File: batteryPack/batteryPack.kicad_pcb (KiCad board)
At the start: 2 copper layers, 210.8 x 83 mm, 38 parts, among them J1 Mirco USB, J10 B1+, J11 B1-, J12 B2-, J13 B1+, J14 B1-, J15 B2+, J16 B2-, J2 B1+, J3 B1-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

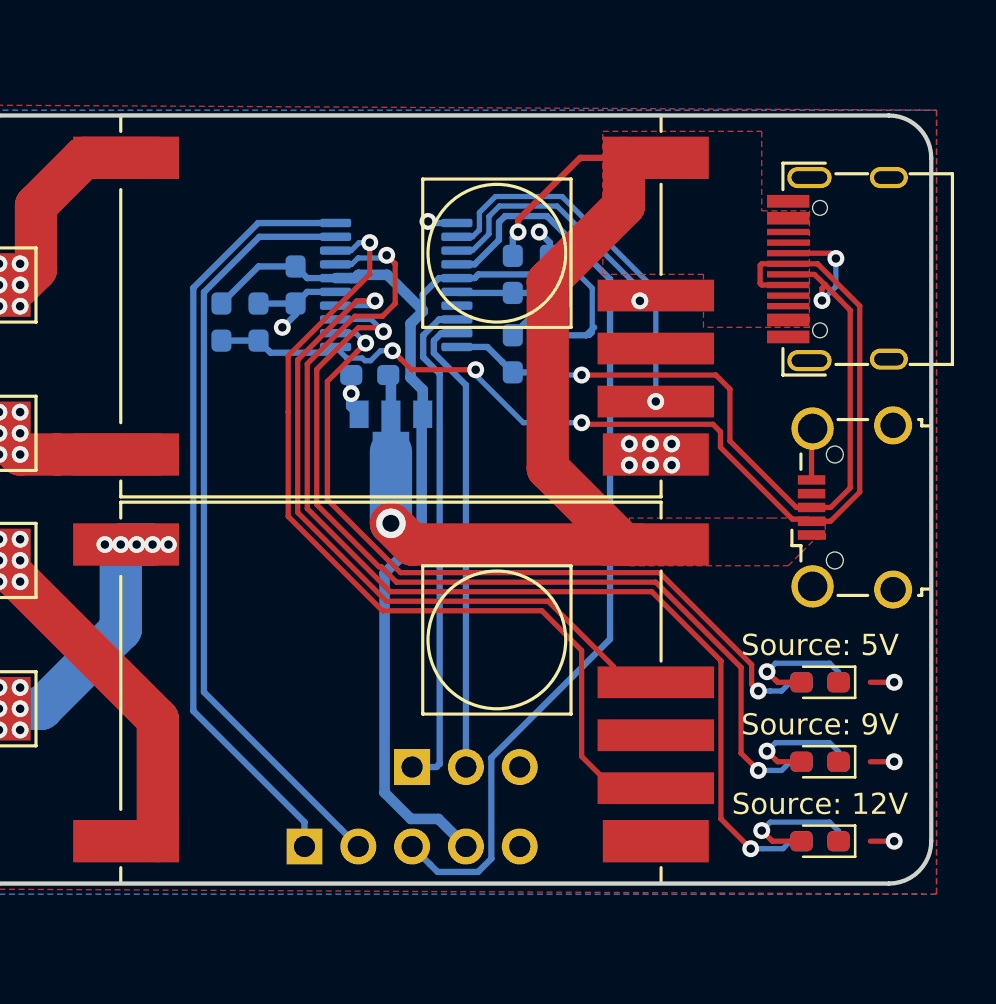
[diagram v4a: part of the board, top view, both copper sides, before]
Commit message: Add battery voltage signalization
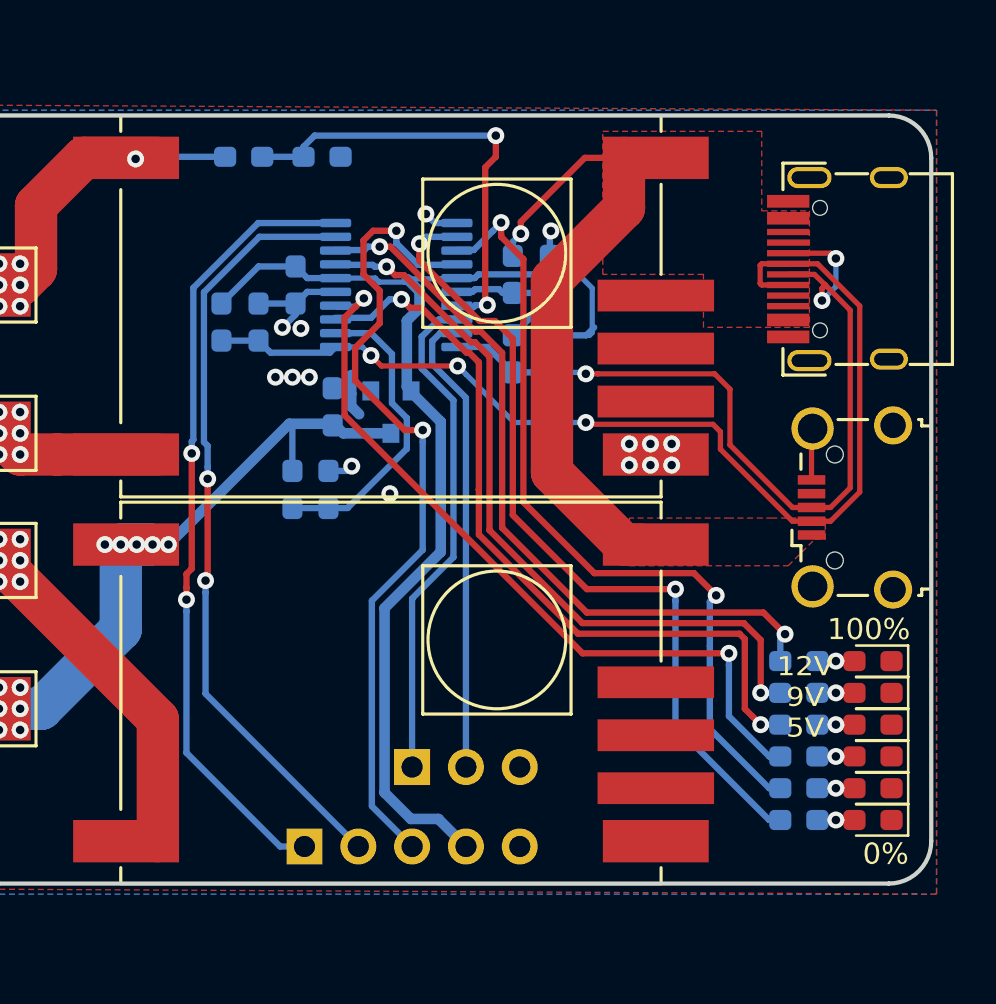
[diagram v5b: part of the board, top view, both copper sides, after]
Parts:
- added D4: LED_40%, LED_SMD:LED_0603_1608Metric_Pad1.05x0.95mm_HandSolder, F.Cu at (231.2, 82.2)
- added D5: LED_20%, LED_SMD:LED_0603_1608Metric_Pad1.05x0.95mm_HandSolder, F.Cu at (231.2, 83.8)
- added D6: LED_0%, LED_SMD:LED_0603_1608Metric_Pad1.05x0.95mm_HandSolder, F.Cu at (231.2, 85.2)
- added R10: 10k, Resistor_SMD:R_0603_1608Metric_Pad1.05x0.95mm_HandSolder, B.Cu at (203.8, 69.7)
- added R11: 20k, Resistor_SMD:R_0603_1608Metric_Pad1.05x0.95mm_HandSolder, B.Cu at (205.6, 69.7)
- added R12: 10k, Resistor_SMD:R_0603_1608Metric_Pad1.05x0.95mm_HandSolder, B.Cu at (201.6, 54.0)
- added R13: 20k, Resistor_SMD:R_0603_1608Metric_Pad1.05x0.95mm_HandSolder, B.Cu at (205.2, 54.0)
- added R14: 1k, Resistor_SMD:R_0603_1608Metric_Pad1.05x0.95mm_HandSolder, B.Cu at (227.8, 82.2)
- added R15: 1k, Resistor_SMD:R_0603_1608Metric_Pad1.05x0.95mm_HandSolder, B.Cu at (227.8, 83.8)
- added R16: 1k, Resistor_SMD:R_0603_1608Metric_Pad1.05x0.95mm_HandSolder, B.Cu at (227.8, 85.2)
- U3: value HT7533-1 -> XC6206P332MR; footprint Package_TO_SOT_SMD:SOT-89-3 -> Package_TO_SOT_SMD:SOT-23
- moved D3 8.86 mm to (231.2, 77.8)
- moved R7 8.56 mm to (227.8, 77.8)
- moved D2 4.10 mm to (231.2, 79.2)
- moved R6 3.40 mm to (227.8, 79.2)
- moved D1 3.20 mm to (231.2, 80.8)
- moved C2 2.30 mm to (205.8, 65.8), turned to 270 degrees
- moved R5 2.24 mm to (227.8, 80.8)
- moved U3 1.75 mm to (208.5, 66.0)
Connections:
- net Net-(J13-Pad1) renamed BAT1+
- C2 pad 2: VBUS -> BAT2+
- J15 pad 1: Net-(J15-Pad1) -> BAT2+
- U1 pad 6: B1_CH -> (no net)
- U1 pad 7: B1_F -> (no net)
- U2 pad 12: Net-(R5-Pad1) -> BAT2_V
- U2 pad 13: Net-(R6-Pad1) -> Net-(R5-Pad1)
- U2 pad 14: B2_F -> Net-(R14-Pad1)
- U2 pad 17: Net-(R7-Pad1) -> Net-(R6-Pad1)
- U2 pad 18: B2_CH -> Net-(R7-Pad1)
- U2 pad 2: B1_CH -> Net-(R16-Pad1)
- U2 pad 3: B1_F -> Net-(R15-Pad1)
- U2 pad 7: (no net) -> BAT1_V
- U3 pad 2: VBUS -> +3V3
- U3 pad 3: +3V3 -> BAT2+
- U4 pad 3: Net-(J15-Pad1) -> BAT2+
- U4 pad 6: B2_CH -> (no net)
- U4 pad 7: B2_F -> (no net)
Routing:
- net B2_CH: track 39.9 -> 0.00 mm, vias 1 -> 0
- net Net-(R16-Pad1): track 0.00 -> 39.3 mm, vias 0 -> 2
- net Net-(R15-Pad1): track 0.00 -> 38.0 mm, vias 0 -> 2
- net Net-(R14-Pad1): track 0.00 -> 36.3 mm, vias 0 -> 2
- net B2_F: track 32.6 -> 0.00 mm, vias 1 -> 0
- net BAT2+: track 0.00 -> 28.2 mm, vias 0 -> 14
- net BAT1_V: track 0.00 -> 21.5 mm, vias 0 -> 2
- net B1_CH: track 19.7 -> 0.00 mm, vias 1 -> 0
- net VBUS: track 46.9 -> 29.8 mm, vias 2 -> 1
- net Net-(R7-Pad1): track 51.7 -> 35.1 mm
- net BAT2_V: track 0.00 -> 14.4 mm
- net B1_F: track 13.5 -> 0.00 mm, vias 1 -> 0
- net Net-(J15-Pad1): track 12.8 -> 0.00 mm, vias 14 -> 0
- net Net-(R6-Pad1): track 43.5 -> 35.7 mm
- net RST: track 44.1 -> 38.7 mm, vias 0 -> 2
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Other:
- board text added: "0%"
- board text added: "100%"
- board text added: "12V 9V 5V"
- board text removed: "Source: 12V"
- board text removed: "Source: 5V"
- board text removed: "Source: 9V"

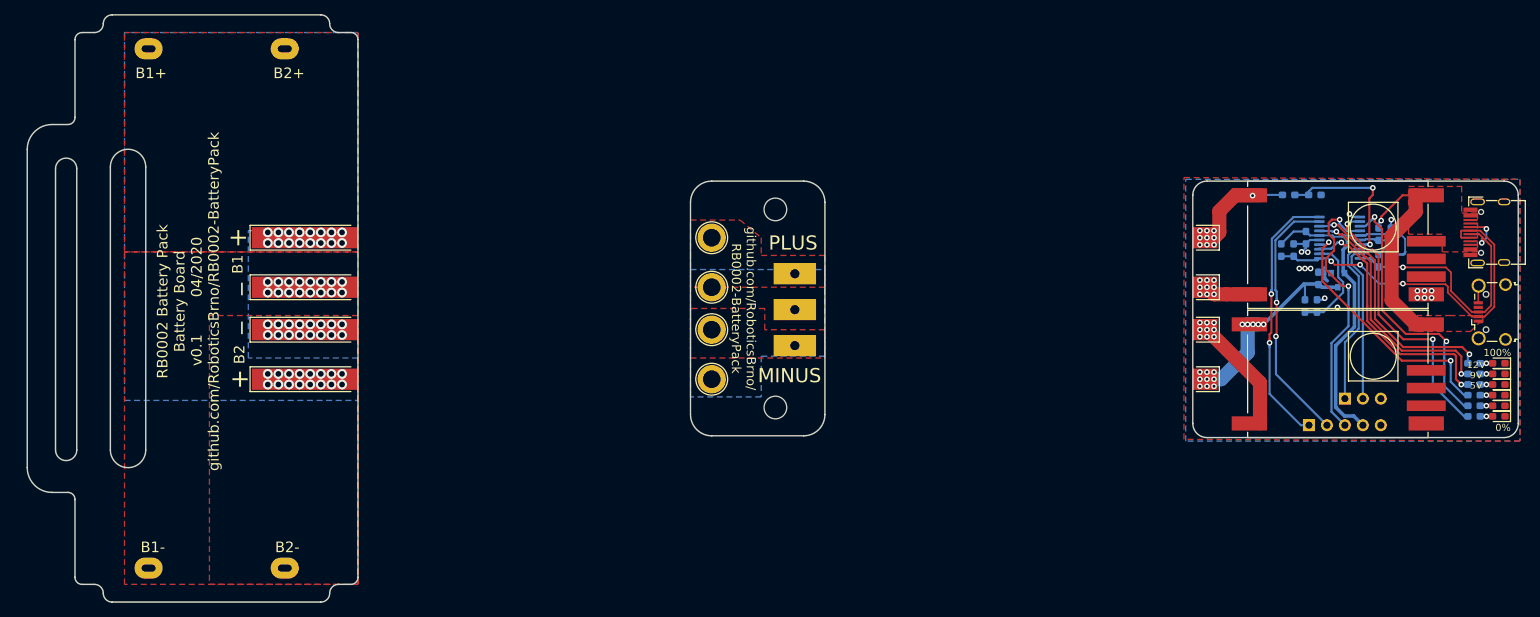
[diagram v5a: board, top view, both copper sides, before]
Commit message: Add silkscreen text + LICENSE
- add version info text to Charger board
- add +/- text for Charger and Connector board
- add license Creative Commons BY-SA 4.0
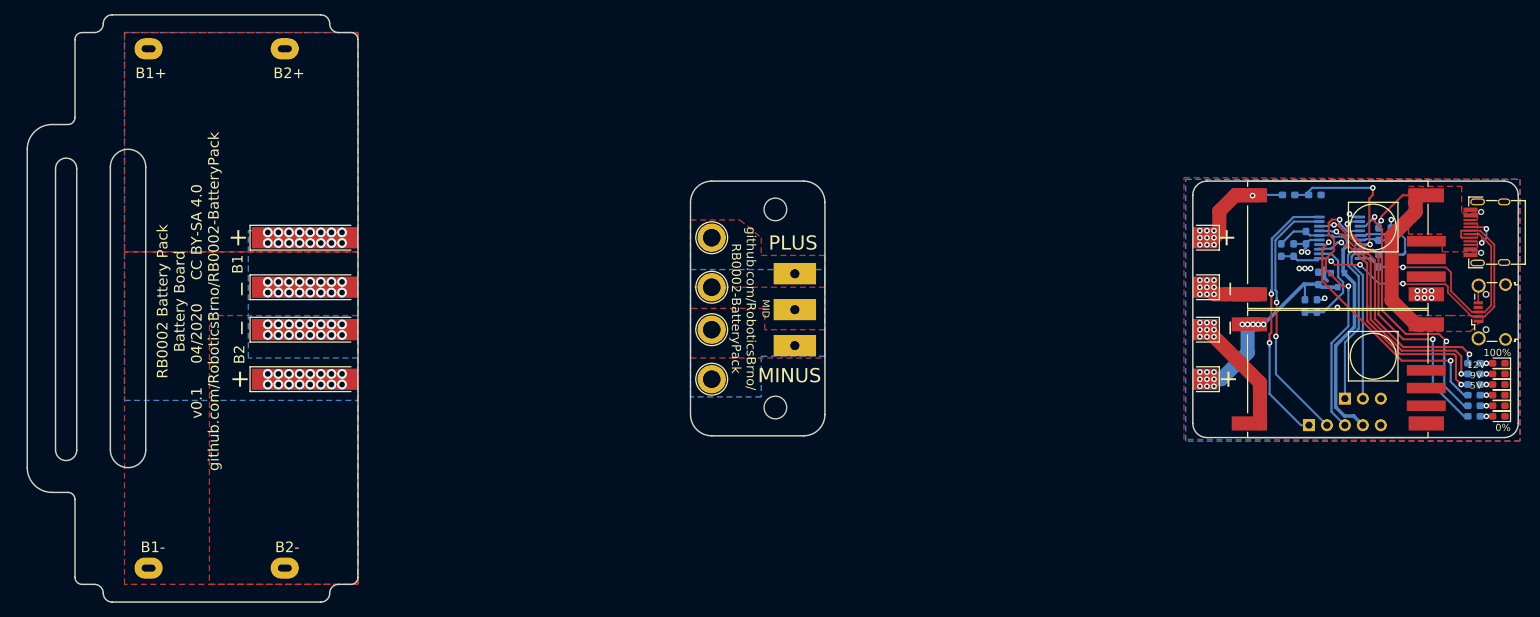
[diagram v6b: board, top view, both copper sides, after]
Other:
- rule trace_min: 0.2 -> 0.1
- rule via_min_size: 0.4 -> 0.35
- board text added: "-"
- board text added: "MID"
- board text added: "RB0002 Battery Pack Battery Board v0.1 04/2020 CC BY-SA 4.0 github.com/RoboticsBrno/RB0002-BatteryPack"
- board text added: "RB0002 Battery Pack Charger v0.1 04/2020"
- board text added: "github.com/RoboticsBrno/ RB0002-BatteryPack CC BY-SA 4.0"
- board text removed: "RB0002 Battery Pack Battery Board v0.1 04/2020 github.com/RoboticsBrno/RB0002-BatteryPack"
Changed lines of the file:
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@@
-(kicad_pcb (version 20171130) (host pcbnew 5.1.5+dfsg1-2build2)
+(kicad_pcb (version 20171130) (host pcbnew "(5.1.5)-3")
   (general
     (thickness 1.6)
-    (drawings 138)
+    (drawings 146)
     (tracks 487)
     (zones 0)
@@
     (zone_clearance 1)
     (zone_45_only no)
-    (trace_min 0.2)
+    (trace_min 0.1)
     (via_size 0.8)
     (via_drill 0.4)
-    (via_min_size 0.4)
+    (via_min_size 0.35)
     (via_min_drill 0.3)
     (user_via 0.8 0.4)
@@
     (aux_axis_origin 0 0)
     (grid_origin 206.25 59.75)
-    (visible_elements FFFFFF7F)
+    (visible_elements 7FFFFFFF)
     (pcbplotparams
       (layerselection 0x010fc_ffffffff)
@@
     )
   )
+  (gr_text MID (at 127.637 70.037 270) (layer F.SilkS)
+    (effects (font (size 1 1) (thickness 0.25)))
+  )
+  (gr_text - (at 131.955 79.435) (layer B.SilkS)
+    (effects (font (size 2 2) (thickness 0.4)) (justify mirror))
+  )
+  (gr_text + (at 131.574 60.766) (layer B.SilkS)
+    (effects (font (size 2 2) (thickness 0.4)) (justify mirror))
+  )
+  (gr_text "RB0002 Battery Pack\nCharger\n v0.1 04/2020" (at 221.49 69.91 270) (layer B.SilkS)
+    (effects (font (size 1.5 1.5) (thickness 0.3)) (justify mirror))
+  )
+  (gr_text + (at 192.95 80 90) (layer F.SilkS)
+    (effects (font (size 2.5 2.5) (thickness 0.5)))
+  )
+  (gr_text + (at 192.7 60 90) (layer F.SilkS)
+    (effects (font (size 2.5 2.5) (thickness 0.5)))
+  )
+  (gr_text _ (at 191.45 72.75 90) (layer F.SilkS)
+    (effects (font (size 2.5 2.5) (thickness 0.5)))
+  )
+  (gr_text _ (at 191.45 67.25 90) (layer F.SilkS)
+    (effects (font (size 2.5 2.5) (thickness 0.5)))
+  )
   (gr_text 0% (at 231.85 86.85) (layer F.SilkS)
     (effects (font (size 1 1) (thickness 0.15)))
@@
   (gr_arc (start 190 54) (end 190 52) (angle -90) (layer Edge.Cuts) (width 0.2))
   (gr_arc (start 232 54) (end 234 54) (angle -90) (layer Edge.Cuts) (width 0.2))
-  (gr_text "github.com/RoboticsBrno/\nRB0002-BatteryPack" (at 197 69 270) (layer B.SilkS)
+  (gr_text "github.com/RoboticsBrno/\nRB0002-BatteryPack\nCC BY-SA 4.0" (at 195.709 70.037 270) (layer B.SilkS)
     (effects (font (size 1.5 1.5) (thickness 0.3)) (justify mirror))
   )
@@
   (gr_arc (start 31 108) (end 30 108) (angle -90) (layer Edge.Cuts) (width 0.2))
   (gr_arc (start 69 108) (end 69 109) (angle -90) (layer Edge.Cuts) (width 0.2))
-  (gr_text "RB0002 Battery Pack\nBattery Board\nv0.1        04/2020\ngithub.com/RoboticsBrno/RB0002-BatteryPack" (at 46 69 90) (layer F.SilkS)
+  (gr_text "RB0002 Battery Pack\nBattery Board\nv0.1     04/2020     CC BY-SA 4.0\ngithub.com/RoboticsBrno/RB0002-BatteryPack" (at 46 69 90) (layer F.SilkS)
     (effects (font (size 1.5 1.5) (thickness 0.3)))
   )

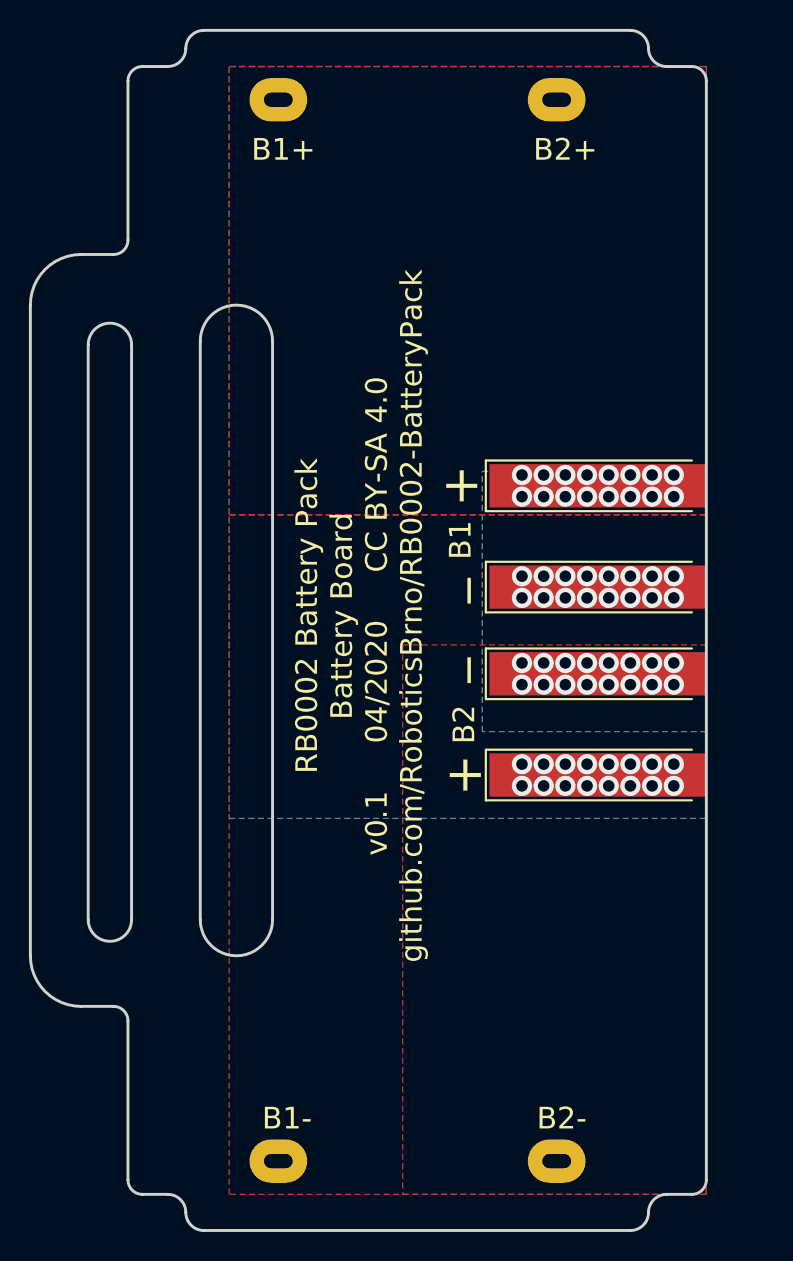
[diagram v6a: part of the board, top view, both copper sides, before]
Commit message: Remove tenons from the battery
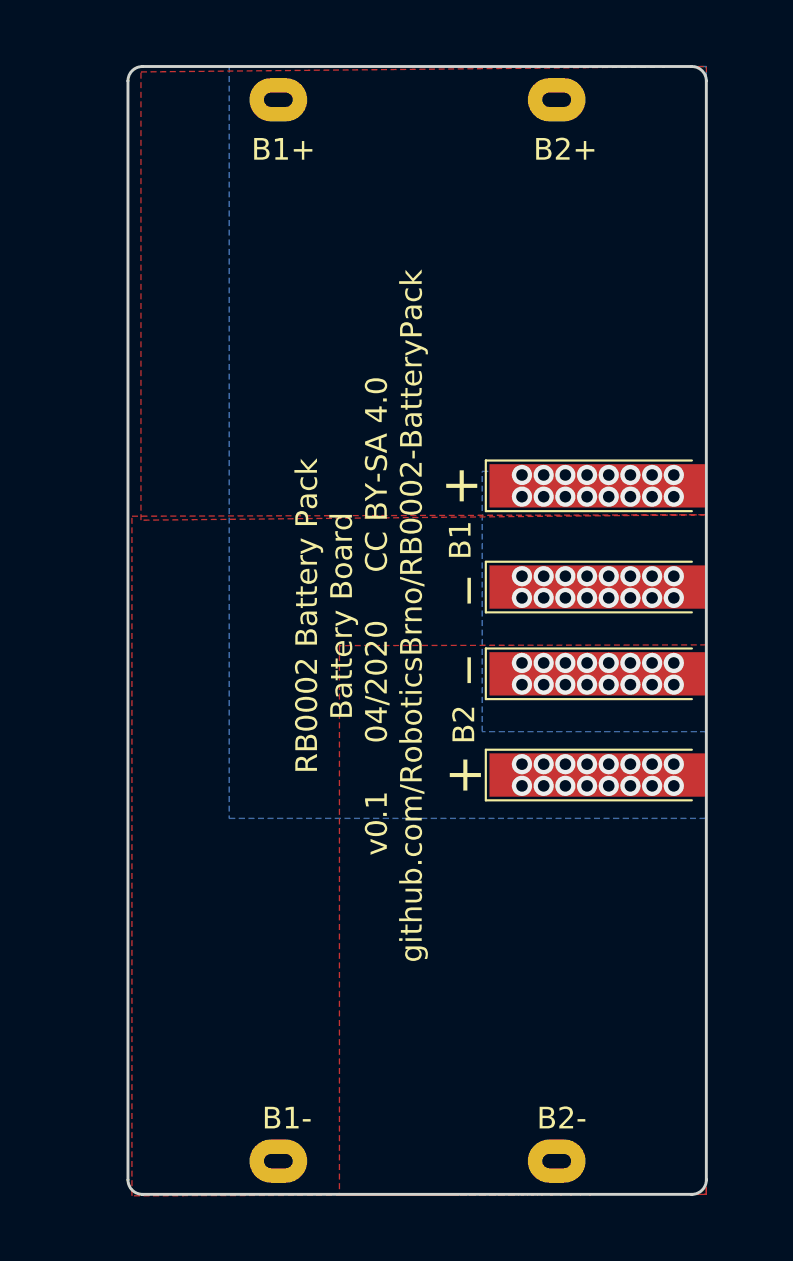
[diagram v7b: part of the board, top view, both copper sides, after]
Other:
- board size 210.8 x 83 mm -> 204 x 78 mm
- board text removed: "Pull-out strip cutout"
